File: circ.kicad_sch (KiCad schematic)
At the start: 2 parts, among them U15 WH3538X-1

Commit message: date update
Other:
- title: M17 Remote Radio Unit - RF board -> Remote Radio Unit - RF board
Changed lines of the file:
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@@
   (paper "A3")
   (title_block
-    (title "M17 Remote Radio Unit - RF board")
-    (date "28-10-2023")
+    (title "Remote Radio Unit - RF board")
+    (date "30-10-2023")
     (rev "A")
     (company "M17 Project")

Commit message: MPN/PN update
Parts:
- R43: MPN (none) -> J100N50X4B
- U15: MPN (none) -> WH3538X-1
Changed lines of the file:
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@@
+      (effects (font (size 1.27 1.27)) hide)
+    )
+    (property "MPN" "J100N50X4B" (at 203.2 154.94 0)
       (effects (font (size 1.27 1.27)) hide)
     )
@@
       (effects (font (size 1.27 1.27)) hide)
     )
+    (property "MPN" "WH3538X-1" (at 203.2 127 0)
+      (effects (font (size 1.27 1.27)) hide)
+    )

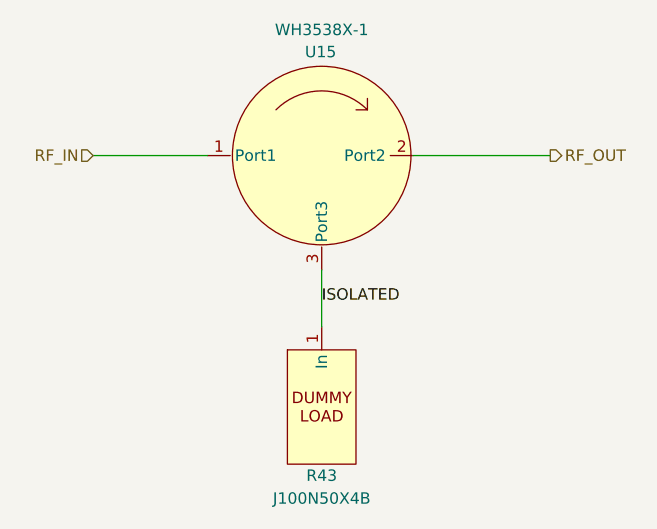
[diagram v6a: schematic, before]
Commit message: WIP rev B
- replaced R44-R46 with 22k
- exposed BOOT0 at the DA15 connector
- added a testpoint at DAC OUT2
- added a buffer to the 40MHz reference oscillator
- removed C2
- bypassed R5 with a 100nF capacitor
- changed D5's voltage to 5.1V
- routed TX_SAMP_CLK
- changed temperature sensor's supply voltage to 5V
- added a series of 100p, 1n and 10n capacitors at PA_VGG
- reduced N-connector cutouts to 2.5mm
- improved RF output track a little
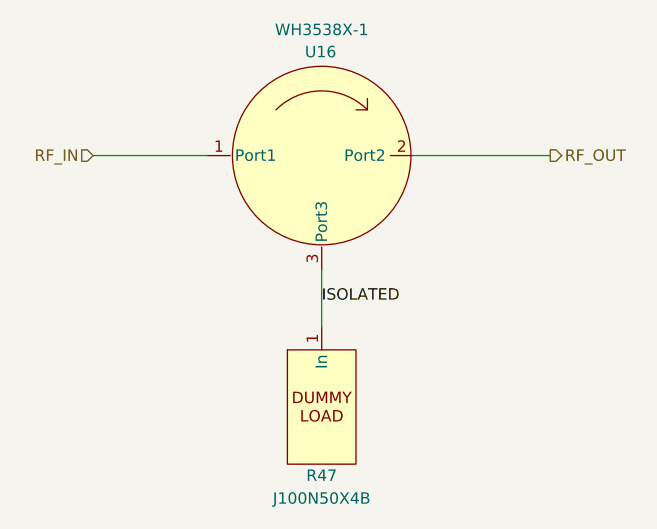
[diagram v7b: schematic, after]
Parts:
- renumbered R43 to R47, U15 to U16
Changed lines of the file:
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@@
   (title_block
     (title "Remote Radio Unit - RF board")
-    (date "10-11-2023")
-    (rev "A")
+    (date "18-01-2024")
+    (rev "B")
     (company "M17 Project")
     (comment 1 "Wojciech Kaczmarski, SP5WWP")
@@
   (symbol (lib_id "Parts:J100N50X4B") (at 203.2 154.94 0) (unit 1)
     (in_bom yes) (on_board yes) (dnp no)
-    (property "Reference" "R43" (at 203.2 162.56 0)
+    (property "Reference" "R47" (at 203.2 162.56 0)
       (effects (font (size 1.27 1.27)))
     )
@@
       (project "m17-rru-rf"
         (path "/4c42207c-9e6b-42da-ad38-da126b892014/52ad0992-68c2-4318-a1ac-e7f0506bc4fb"
-          (reference "R43") (unit 1)
+          (reference "R47") (unit 1)
         )
       )
@@
   (symbol (lib_id "Parts:WH3538X-1") (at 203.2 127 0) (unit 1)
     (in_bom yes) (on_board yes) (dnp no) (fields_autoplaced)
-    (property "Reference" "U15" (at 203.0795 115.4879 0)
+    (property "Reference" "U16" (at 203.0795 115.4879 0)
       (effects (font (size 1.27 1.27)))
     )
@@
       (project "m17-rru-rf"
         (path "/4c42207c-9e6b-42da-ad38-da126b892014/52ad0992-68c2-4318-a1ac-e7f0506bc4fb"
-          (reference "U15") (unit 1)
+          (reference "U16") (unit 1)
         )
       )

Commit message: WIP rev B
- added bleed resistors
- power supply now uses linear regulators
- routed RX_SAMP_CLK
- added some decoupling at RF_PA_VDD
- added some GND vias here and there
- updated BOM
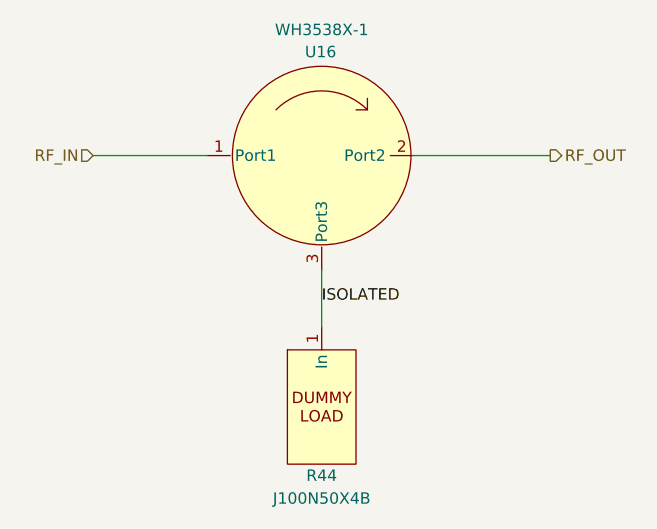
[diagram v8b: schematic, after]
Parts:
- renumbered R47 to R44
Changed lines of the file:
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@@
   (title_block
     (title "Remote Radio Unit - RF board")
-    (date "18-01-2024")
+    (date "19-01-2024")
     (rev "B")
     (company "M17 Project")
@@
   (symbol (lib_id "Parts:J100N50X4B") (at 203.2 154.94 0) (unit 1)
     (in_bom yes) (on_board yes) (dnp no)
-    (property "Reference" "R47" (at 203.2 162.56 0)
+    (property "Reference" "R44" (at 203.2 162.56 0)
       (effects (font (size 1.27 1.27)))
     )
@@
       (project "m17-rru-rf"
         (path "/4c42207c-9e6b-42da-ad38-da126b892014/52ad0992-68c2-4318-a1ac-e7f0506bc4fb"
-          (reference "R47") (unit 1)
+          (reference "R44") (unit 1)
         )
       )
